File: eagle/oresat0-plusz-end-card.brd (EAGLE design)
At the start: 99.8 x 94.6 mm, 42 parts, among them J1 Harwin M55-7101242R, J10 R107064070_CONTACT, J11 R107064070_CONTACT, J12 R107064070_CONTACT, J13 R107064070_CONTACT, J14 R107064070_CONTACT, J15 R107064070_CONTACT, J16 R107064070_CONTACT, J2 Harwin M55-7101242R, J3 Harwin M55-7101242R, J4 Harwin M55-7101242R, J6 J-SAMTEC-TFM-120-X1-XXX-D-RA, J7 R107064070_CONTACT, J8 R107064070_CONTACT, J9 R107064070_CONTACT, U1 QCN-19+, U2 QCN-19+, U3 QCN-19+

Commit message: replaced S-band net labels with L1-band labels, swapped the S-band hybrids with L-band hybrids, recalculated 1/4 wavelength trace length, routed a new short+1/4 wavelength trace
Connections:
- net SBAND renamed L1BAND
- net SBAND_0 renamed L1BAND_0
- net SBAND_180 renamed L1BAND_180
- net SBAND_270 renamed L1BAND_270
- net SBAND_90 renamed L1BAND_90
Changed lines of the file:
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@@
 <layer number="13" name="Route13" color="21" fill="1" visible="no" active="no"/>
 <layer number="14" name="Route14" color="22" fill="1" visible="no" active="no"/>
-<layer number="15" name="Route15" color="23" fill="1" visible="no" active="yes"/>
-<layer number="16" name="Bottom" color="1" fill="1" visible="no" active="yes"/>
+<layer number="15" name="Route15" color="23" fill="1" visible="yes" active="yes"/>
+<layer number="16" name="Bottom" color="1" fill="1" visible="yes" active="yes"/>
 <layer number="17" name="Pads" color="2" fill="1" visible="yes" active="yes"/>
 <layer number="18" name="Vias" color="2" fill="1" visible="yes" active="yes"/>
@@
 <layer number="20" name="Dimension" color="24" fill="1" visible="yes" active="yes"/>
 <layer number="21" name="tPlace" color="7" fill="1" visible="yes" active="yes"/>
-<layer number="22" name="bPlace" color="7" fill="1" visible="no" active="yes"/>
+<layer number="22" name="bPlace" color="7" fill="1" visible="yes" active="yes"/>
 <layer number="23" name="tOrigins" color="15" fill="1" visible="yes" active="yes"/>
-<layer number="24" name="bOrigins" color="15" fill="1" visible="no" active="yes"/>
+<layer number="24" name="bOrigins" color="15" fill="1" visible="yes" active="yes"/>
 <layer number="25" name="tNames" color="7" fill="1" visible="no" active="yes"/>
 <layer number="26" name="bNames" color="7" fill="1" visible="no" active="yes"/>
@@
 <layer number="50" name="dxf" color="11" fill="1" visible="no" active="yes"/>
 <layer number="51" name="tDocu" color="7" fill="1" visible="yes" active="yes"/>
-<layer number="52" name="bDocu" color="7" fill="1" visible="no" active="yes"/>
+<layer number="52" name="bDocu" color="7" fill="1" visible="yes" active="yes"/>
 <layer number="53" name="tGND_GNDA" color="7" fill="9" visible="no" active="no"/>
 <layer number="54" name="bGND_GNDA" color="1" fill="9" visible="no" active="no"/>
@@
 <contactref element="CM3" pad="RF"/>
 </signal>
-<signal name="SBAND_270" class="1">
+<signal name="L1BAND_270" class="1">
 <contactref element="J13" pad="P$1"/>
 <via x="77.3" y="65.2" extent="1-16" drill="1"/>
@@
 <wire x1="77.300003125" y1="65.2" x2="77.3" y2="65.2" width="0.38" layer="16"/>
 </signal>
-<signal name="SBAND_180" class="1">
+<signal name="L1BAND_180" class="1">
 <contactref element="J14" pad="P$1"/>
 <via x="34.5" y="77.2" extent="1-16" drill="1" locked="yes"/>
 <wire x1="34.5" y1="77.2" x2="33.04853125" y2="78.65146875" width="0.38" layer="16"/>
 </signal>
-<signal name="SBAND_90" class="1">
+<signal name="L1BAND_90" class="1">
 <contactref element="J15" pad="P$1"/>
 <via x="22.5" y="34.4" extent="1-16" drill="1" locked="yes"/>
 <wire x1="22.5" y1="34.4" x2="21.04853125" y2="32.948528125" width="0.38" layer="16"/>
 </signal>
-<signal name="SBAND_0" class="1">
+<signal name="L1BAND_0" class="1">
 <contactref element="J16" pad="P$1"/>
 <via x="65.3" y="22.4" extent="1-16" drill="1" locked="yes"/>
 <wire x1="65.3" y1="22.4" x2="66.751471875" y2="20.948528125" width="0.38" layer="16"/>
 </signal>
-<signal name="SBAND" class="1">
+<signal name="L1BAND" class="1">
 <contactref element="CM1" pad="RF"/>
 <contactref element="J12" pad="P$1"/>

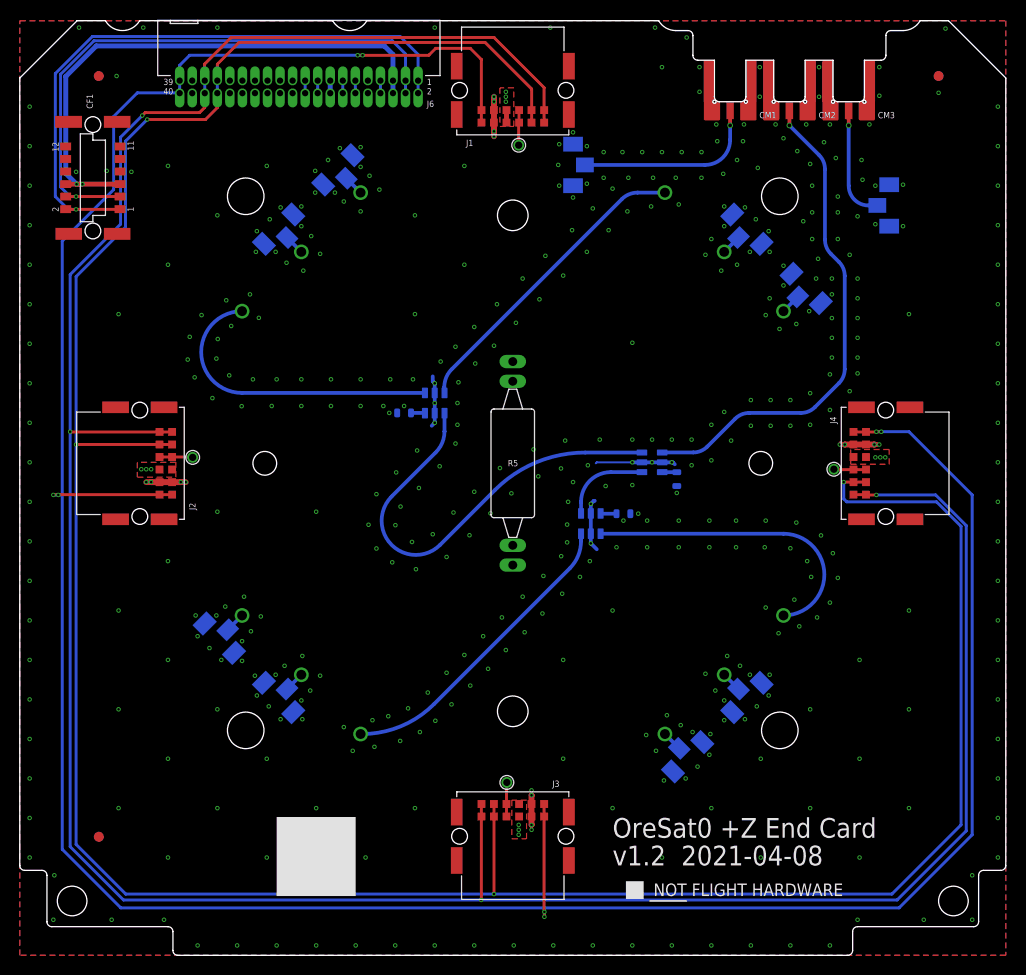
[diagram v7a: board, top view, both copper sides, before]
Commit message: v2.0 card, mezzanine, and BOM for v2.0. Moved UHF hybrids to avoid melt wire resistor leads. Updated BOM to reflect new v2.0 design.
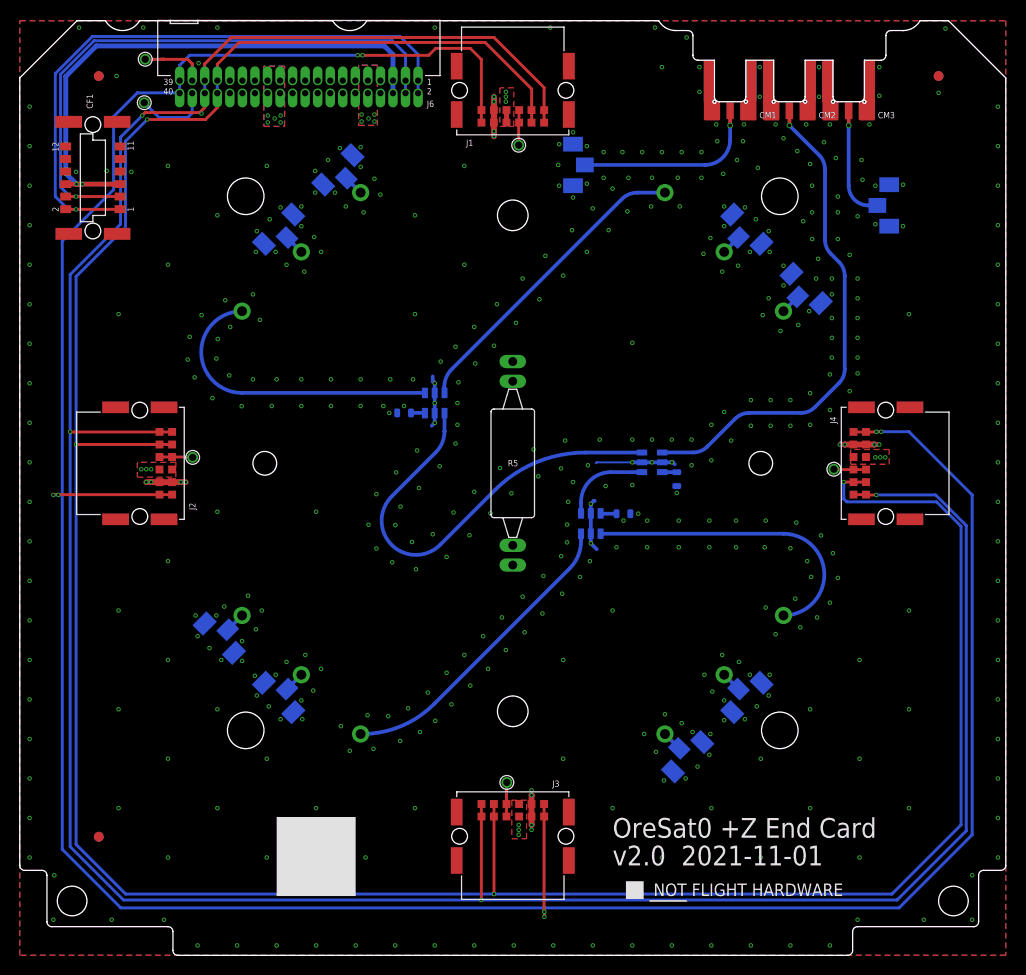
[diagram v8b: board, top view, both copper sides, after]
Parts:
- added TP5, TP6: TEST-POINT-LARGE-SQUARE, oresat-misc:1X01
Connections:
- removed net CAN2_H: J6.17, J6.18
- removed net CAN2_L: J6.19, J6.20
- removed net OPD_PWR: J6.15, J6.16
- removed net OPD_SCL: J6.13, J6.14
- removed net OPD_SDA: J6.11, J6.12
- removed net SPARE2: J6.7, J6.8
- new net C3-UART-RX: J6.38, TP5.1
- new net C3-UART-TX: J6.37, TP6.1
- net GND: no longer J6.31, J6.32, J6.37, J6.38
- net VBUS: no longer J6.21, J6.22
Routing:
- net C3-UART-RX: track 0.00 -> 7.67 mm
- net C3-UART-TX: track 0.00 -> 6.95 mm
- net SPARE2: track 1.27 -> 0.00 mm
- net OPD_SDA: track 1.27 -> 0.00 mm
- net OPD_SCL: track 1.27 -> 0.00 mm
- net OPD_PWR: track 1.27 -> 0.00 mm
- net CAN2_L: track 1.27 -> 0.00 mm
- net CAN2_H: track 1.27 -> 0.00 mm
- net VBUS: vias 12 -> 17
- net GND: vias 454 -> 456
- added copper zone on layer 1, net TURNSTILE-DEPLOY
- added copper zone on layer 16, net TURNSTILE-DEPLOY
- added copper zone on layer 16, net VBUS
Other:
- board text added: "v2.0 2021-11-01"
- board text removed: "v1.2 2021-04-08"
